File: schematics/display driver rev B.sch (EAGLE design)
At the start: 78 parts, among them U1 ATF1502AS, U10 TLC5916IN, U11 TLC5916IN, U12 TLC5916IN, U13 TLC5916IN, U14 TLC5916IN, U15 TLC5916IN, U16 TLC5916IN, U17 TLC5916IN, U18 TLC5916IN, U19 TLC5916IN, U2 74LS688N, U20 TLC5916IN, U21 TLC5916IN, U22 TLC5916IN, U23 TLC5916IN, U24 TLC5916IN, U3 74HC688, U4 74HC32, U5 74HC00, U6 74HC573N, U7 74HC138, U8 TLC5916IN, U9 TLC5916IN

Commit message: Display driver PCB layout
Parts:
- removed SV1, SV2, SV3, SV4: (no value), con-ml:ML40E
- added CN1, CN2, CN3, CN4: (no value), Z80 clock:HDR40
- BUS: device con-ml:ML40E -> Z80 clock:HDR40
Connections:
- net +5V: now also CN4-38.S, CN4-40.S; no longer SV4-38.S, SV4-40.S
- net A1: now also U2A.P7, U3A.P7; no longer U2A.P1, U3A.P1
- net A2: now also U2A.P1, U3A.P1; no longer U2A.P2, U3A.P2
- net A3: now also U2A.P6, U3A.P6; no longer U2A.P3, U3A.P3
- net A4: now also U2A.P2, U3A.P2; no longer U2A.P4, U3A.P4
- net A6: now also U2A.P3, U3A.P3; no longer U2A.P6, U3A.P6
- net A7: now also U2A.P4, U3A.P4; no longer U2A.P7, U3A.P7
- net COL0_A: now also CN1-16.S; no longer SV1-9.S
- net COL0_B: now also CN1-17.S; no longer SV1-24.S
- net COL0_C: now also CN1-19.S; no longer SV1-22.S
- net COL0_D: now also CN1-22.S; no longer SV1-19.S
- net COL0_E: now also CN1-23.S; no longer SV1-18.S
- net COL0_F: now also CN1-24.S; no longer SV1-17.S
- net COL0_G: now also CN1-9.S; no longer SV1-16.S
- net COL0_H: now also CN1-13.S; no longer SV1-12.S
- net COL0_K: now also CN1-14.S; no longer SV1-11.S
- net COL0_M: now also CN1-15.S; no longer SV1-10.S
- net COL0_N: now also CN1-18.S; no longer SV1-23.S
- net COL0_P: now also CN1-20.S; no longer SV1-21.S
- net COL0_R: now also CN1-21.S; no longer SV1-20.S
- net COL0_S: now also CN1-11.S; no longer SV1-14.S
- net COL0_T: now also CN1-10.S; no longer SV1-15.S
- net COL0_U: now also CN1-12.S; no longer SV1-13.S
- net COL1_A: now also CN3-5.S; no longer SV3-1.S
- net COL1_B: now also CN3-12.S; no longer SV3-16.S
- net COL1_C: now also CN3-10.S; no longer SV3-14.S
- net COL1_D: now also CN3-15.S; no longer SV3-11.S
- net COL1_E: now also CN3-14.S; no longer SV3-10.S
- net COL1_F: now also CN3-13.S; no longer SV3-9.S
- net COL1_G: now also CN3-4.S; no longer SV3-8.S
- net COL1_H: now also CN3-8.S; no longer SV3-4.S
- net COL1_K: now also CN3-7.S; no longer SV3-3.S
- net COL1_M: now also CN3-6.S; no longer SV3-2.S
- net COL1_N: now also CN3-11.S; no longer SV3-15.S
- net COL1_P: now also CN3-9.S; no longer SV3-13.S
- net COL1_R: now also CN3-16.S; no longer SV3-12.S
- net COL1_S: now also CN3-2.S; no longer SV3-6.S
- net COL1_T: now also CN3-3.S; no longer SV3-7.S
- net COL1_U: now also CN3-1.S; no longer SV3-5.S
- net COL2_A: now also CN1-32.S; no longer SV1-25.S
- net COL2_B: now also CN1-33.S; no longer SV1-40.S
- net COL2_C: now also CN1-35.S; no longer SV1-38.S
- net COL2_D: now also CN1-38.S; no longer SV1-35.S
- net COL2_E: now also CN1-39.S; no longer SV1-34.S
- net COL2_F: now also CN1-40.S; no longer SV1-33.S
- net COL2_G: now also CN1-25.S; no longer SV1-32.S
- net COL2_H: now also CN1-29.S; no longer SV1-28.S
- net COL2_K: now also CN1-30.S; no longer SV1-27.S
- net COL2_M: now also CN1-31.S; no longer SV1-26.S
- net COL2_N: now also CN1-34.S; no longer SV1-39.S
- net COL2_P: now also CN1-36.S; no longer SV1-37.S
- net COL2_R: now also CN1-37.S; no longer SV1-36.S
- net COL2_S: now also CN1-27.S; no longer SV1-30.S
- net COL2_T: now also CN1-26.S; no longer SV1-31.S
- net COL2_U: now also CN1-28.S; no longer SV1-29.S
- net COL3_A: now also CN3-29.S; no longer SV3-25.S
- net COL3_B: now also CN3-36.S; no longer SV3-40.S
- net COL3_C: now also CN3-34.S; no longer SV3-38.S
- net COL3_D: now also CN3-39.S; no longer SV3-35.S
- net COL3_E: now also CN3-38.S; no longer SV3-34.S
- net COL3_F: now also CN3-37.S; no longer SV3-33.S
- net COL3_G: now also CN3-28.S; no longer SV3-32.S
- net COL3_H: now also CN3-32.S; no longer SV3-28.S
- net COL3_K: now also CN3-31.S; no longer SV3-27.S
- net COL3_M: now also CN3-30.S; no longer SV3-26.S
- net COL3_N: now also CN3-35.S; no longer SV3-39.S
- net COL3_P: now also CN3-33.S; no longer SV3-37.S
- net COL3_R: now also CN3-40.S; no longer SV3-36.S
- net COL3_S: now also CN3-26.S; no longer SV3-30.S
- net COL3_T: now also CN3-27.S; no longer SV3-31.S
- net COL3_U: now also CN3-25.S; no longer SV3-29.S
- net COL4_A: now also CN2-8.S; no longer SV2-1.S
- net COL4_B: now also CN2-9.S; no longer SV2-16.S
- net COL4_C: now also CN2-11.S; no longer SV2-14.S
- net COL4_D: now also CN2-14.S; no longer SV2-11.S
- net COL4_E: now also CN2-15.S; no longer SV2-10.S
- net COL4_F: now also CN2-16.S; no longer SV2-9.S
- net COL4_G: now also CN2-1.S; no longer SV2-8.S
- net COL4_H: now also CN2-5.S; no longer SV2-4.S
- net COL4_K: now also CN2-6.S; no longer SV2-3.S
- net COL4_M: now also CN2-7.S; no longer SV2-2.S
- net COL4_N: now also CN2-10.S; no longer SV2-15.S
- net COL4_P: now also CN2-12.S; no longer SV2-13.S
- net COL4_R: now also CN2-13.S; no longer SV2-12.S
- net COL4_S: now also CN2-3.S; no longer SV2-6.S
- net COL4_T: now also CN2-2.S; no longer SV2-7.S
- net COL4_U: now also CN2-4.S; no longer SV2-5.S
- net COL5_A: now also CN4-5.S; no longer SV4-1.S
- net COL5_B: now also CN4-12.S; no longer SV4-16.S
- net COL5_C: now also CN4-10.S; no longer SV4-14.S
- net COL5_D: now also CN4-15.S; no longer SV4-11.S
- net COL5_E: now also CN4-14.S; no longer SV4-10.S
- net COL5_F: now also CN4-13.S; no longer SV4-9.S
- net COL5_G: now also CN4-4.S; no longer SV4-8.S
- net COL5_H: now also CN4-8.S; no longer SV4-4.S
- net COL5_K: now also CN4-7.S; no longer SV4-3.S
- net COL5_M: now also CN4-6.S; no longer SV4-2.S
- net COL5_N: now also CN4-11.S; no longer SV4-15.S
- net COL5_P: now also CN4-9.S; no longer SV4-13.S
- net COL5_R: now also CN4-16.S; no longer SV4-12.S
- net COL5_S: now also CN4-2.S; no longer SV4-6.S
- net COL5_T: now also CN4-3.S; no longer SV4-7.S
- net COL5_U: now also CN4-1.S; no longer SV4-5.S
- net COL6_A: now also CN2-24.S; no longer SV2-17.S
- net COL6_B: now also CN2-25.S; no longer SV2-32.S
- net COL6_C: now also CN2-27.S; no longer SV2-30.S
- net COL6_D: now also CN2-30.S; no longer SV2-27.S
- net COL6_E: now also CN2-31.S; no longer SV2-26.S
- net COL6_F: now also CN2-32.S; no longer SV2-25.S
- net COL6_G: now also CN2-17.S; no longer SV2-24.S
- net COL6_H: now also CN2-21.S; no longer SV2-20.S
- net COL6_K: now also CN2-22.S; no longer SV2-19.S
- net COL6_M: now also CN2-23.S; no longer SV2-18.S
- net COL6_N: now also CN2-26.S; no longer SV2-31.S
- net COL6_P: now also CN2-28.S; no longer SV2-29.S
- net COL6_R: now also CN2-29.S; no longer SV2-28.S
- net COL6_S: now also CN2-19.S; no longer SV2-22.S
- net COL6_T: now also CN2-18.S; no longer SV2-23.S
- net COL6_U: now also CN2-20.S; no longer SV2-21.S
- net COL7_A: now also CN2-40.S; no longer SV2-33.S
- net COL7_B: now also CN4-20.S; no longer SV4-24.S
- net COL7_C: now also CN4-18.S; no longer SV4-22.S
- net COL7_D: now also CN4-23.S; no longer SV4-19.S
- net COL7_E: now also CN4-22.S; no longer SV4-18.S
- net COL7_F: now also CN4-21.S; no longer SV4-17.S
- net COL7_G: now also CN2-33.S; no longer SV2-40.S
- net COL7_H: now also CN2-37.S; no longer SV2-36.S
- net COL7_K: now also CN2-38.S; no longer SV2-35.S
- net COL7_M: now also CN2-39.S; no longer SV2-34.S
- net COL7_N: now also CN4-19.S; no longer SV4-23.S
- net COL7_P: now also CN4-17.S; no longer SV4-21.S
- net COL7_R: now also CN4-24.S; no longer SV4-20.S
- net COL7_S: now also CN2-35.S; no longer SV2-38.S
- net COL7_T: now also CN2-34.S; no longer SV2-39.S
- net COL7_U: now also CN2-36.S; no longer SV2-37.S
- net DP0: now also CN1-8.S; no longer SV1-1.S
- net DP1: now also CN1-7.S; no longer SV1-2.S
- net DP2: now also CN1-6.S; no longer SV1-3.S
- net DP3: now also CN1-5.S; no longer SV1-4.S
- net DP4: now also CN1-4.S; no longer SV1-5.S
- net DP5: now also CN1-3.S; no longer SV1-6.S
- net DP6: now also CN1-2.S; no longer SV1-7.S
- net DP7: now also CN1-1.S; no longer SV1-8.S
- net GND: now also CN4-37.S, CN4-39.S; no longer SV4-37.S, SV4-39.S
- net N$3: now also CN4-34.S; no longer SV4-34.S
- net N$6: now also CN4-35.S; no longer SV4-35.S
- net N$7: now also CN4-36.S; no longer SV4-36.S

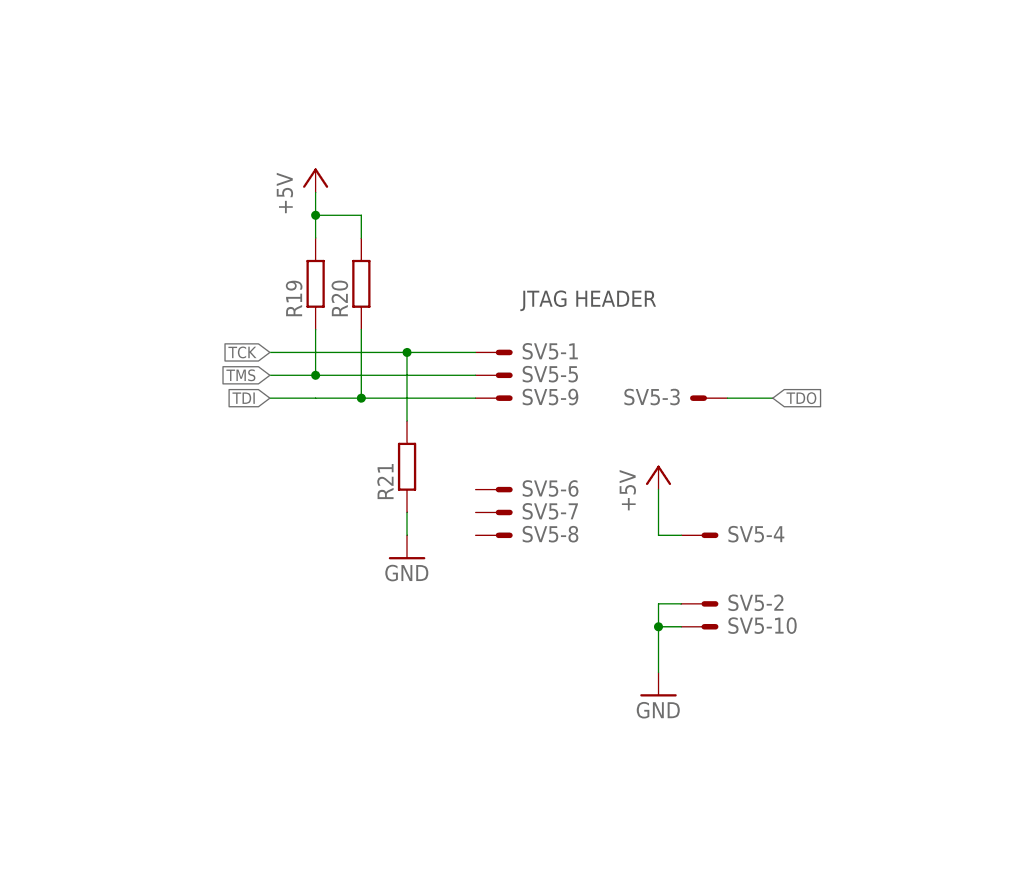
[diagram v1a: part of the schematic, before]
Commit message: Space things out a little more on the board
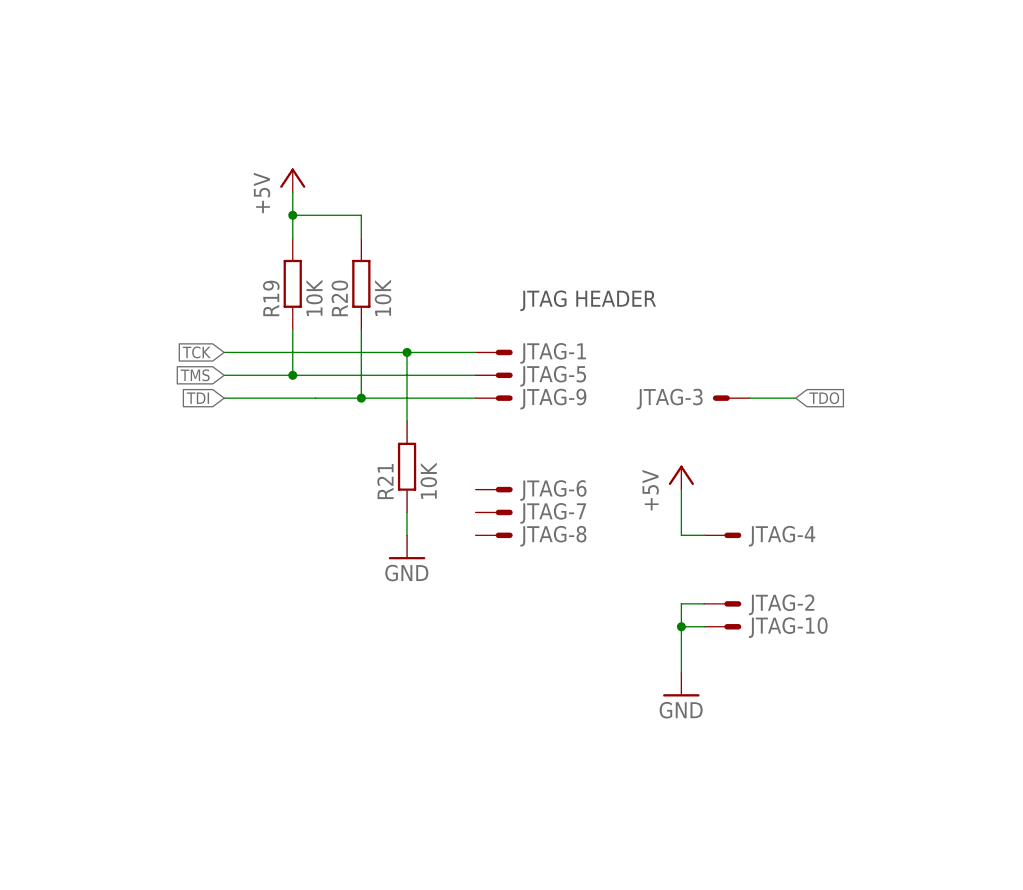
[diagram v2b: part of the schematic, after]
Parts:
- R19, R20, R21: value (none) -> 10K
- renumbered SV5 to JTAG
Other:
- moved on the sheet: R19

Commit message: Tidy up a little
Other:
- note added: "LAYOUT OF SHIFT REGISTERS AND RELATION TO HEADERS AS SEEN FROM BOTTOM OF PROTOTYPE DISPLAY DRIVER BOARD"
- note removed: "LAYOUT OF SHIFT REGISTERS AND RELATION TO HEADERS AS SEEN FROM BOTTOM OF DISPLAY DRIVER BOARD"
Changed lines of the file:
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@@
 <wire x1="513.08" y1="83.82" x2="513.08" y2="73.66" width="0.1524" layer="88"/>
 <wire x1="502.92" y1="86.36" x2="513.08" y2="86.36" width="0.1524" layer="88"/>
-<text x="510.54" y="12.7" size="1.778" layer="97">LAYOUT OF SHIFT REGISTERS AND RELATION TO HEADERS AS SEEN FROM BOTTOM OF DISPLAY
-DRIVER BOARD</text>
+<text x="510.54" y="12.7" size="1.778" layer="97">LAYOUT OF SHIFT REGISTERS AND RELATION TO HEADERS AS SEEN FROM BOTTOM OF
+PROTOTYPE DISPLAY DRIVER BOARD</text>
 <wire x1="518.16" y1="63.5" x2="528.32" y2="63.5" width="0.1524" layer="88"/>
 <wire x1="518.16" y1="48.26" x2="528.32" y2="48.26" width="0.1524" layer="88"/>
